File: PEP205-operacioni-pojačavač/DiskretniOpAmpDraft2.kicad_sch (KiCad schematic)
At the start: 40 parts, among them J1 J111, J2 Ulazi, J3 Izlaz, J4 +9V, J5 GND, J6 -9V, J7 KlasaABIzlaz, J8 J111, Q10 NPN, Q11 NPN, Q12 NPN, Q13 NPN, Q14 PNP, Q3 PNP, Q4 PNP, Q5 NPN, Q6 PNP, Q7 PNP, Q8 PNP, Q9 NPN

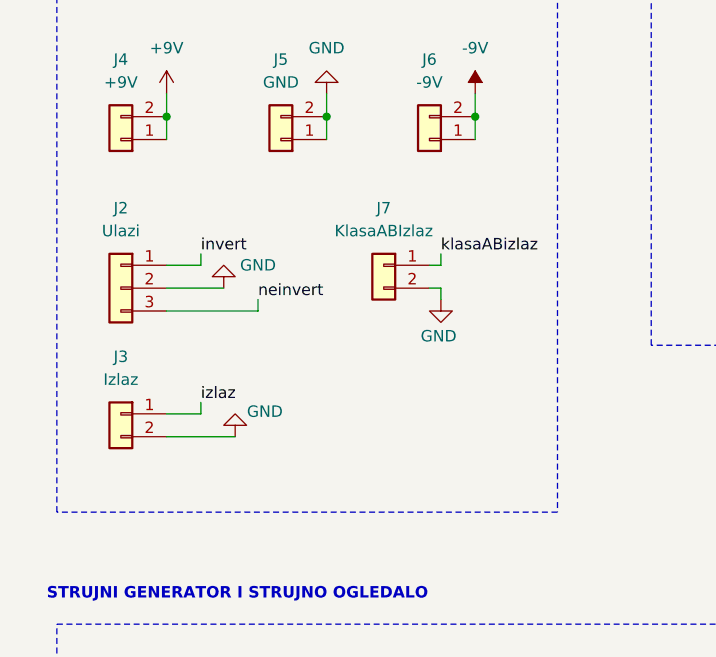
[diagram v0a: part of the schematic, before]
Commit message: zbrzano dodati konektori na drugačiji način
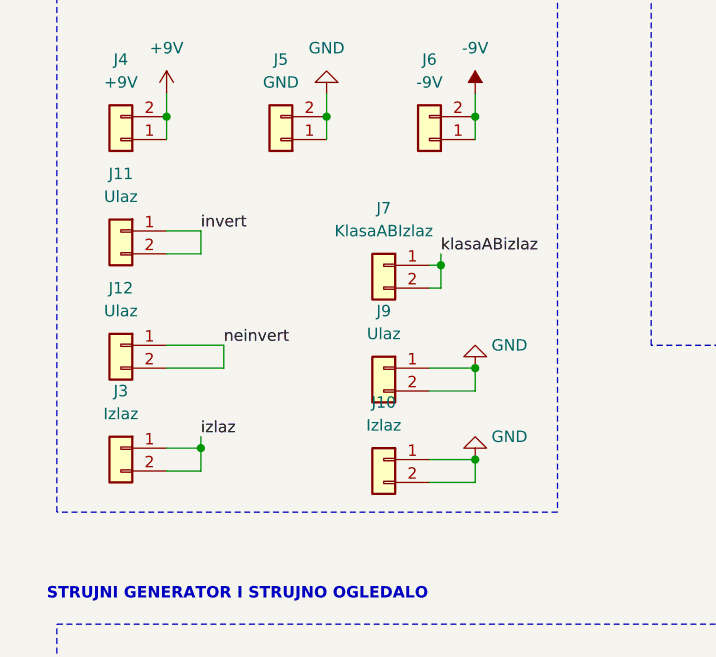
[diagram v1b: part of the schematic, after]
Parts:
- removed J2: Ulazi, Connector_PinSocket_2.54mm:PinSocket_1x03_P2.54mm_Vertical, symbol Connector_Generic:Conn_01x03
- added J10: Izlaz, Connector_PinSocket_2.54mm:PinSocket_1x02_P2.54mm_Vertical, symbol Connector_Generic:Conn_01x02
- added J11, J12, J9: Ulaz, Connector_PinSocket_2.54mm:PinSocket_1x02_P2.54mm_Vertical, symbol Connector_Generic:Conn_01x02
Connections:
- net GND: now also J10.1 (Pin_1), J10.2 (Pin_2), J9.1 (Pin_1), J9.2 (Pin_2); no longer J3.2 (Pin_2), J7.2 (Pin_2)
- net invert: now also J11.1 (Pin_1), J11.2 (Pin_2)
- net izlaz: now also J3.2 (Pin_2)
- net klasaABizlaz: now also J7.2 (Pin_2)
- net neinvert: now also J12.1 (Pin_1), J12.2 (Pin_2)
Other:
- moved on the sheet: J3

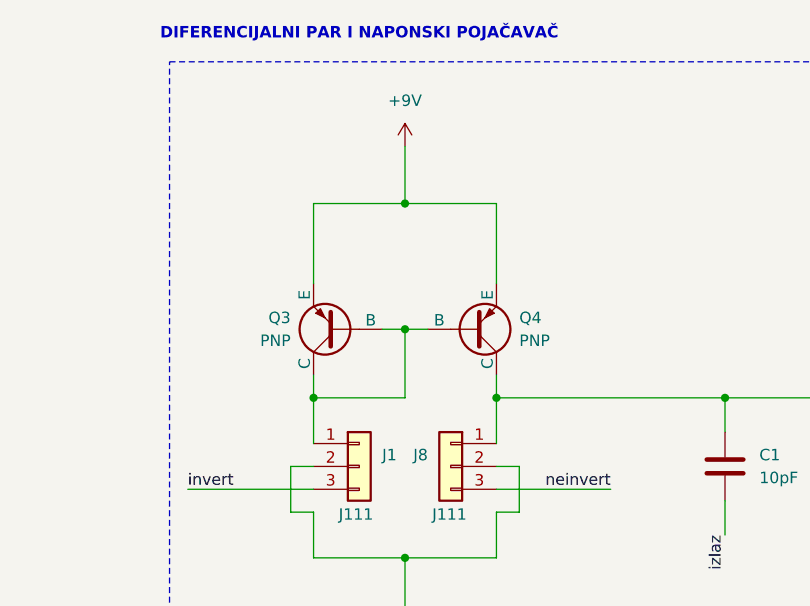
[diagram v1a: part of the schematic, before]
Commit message: Dodat još jedan tranzistor da bi se formiralo Vilsonovo ogledalo sa 3 tranzistora kod diferencijalnog para
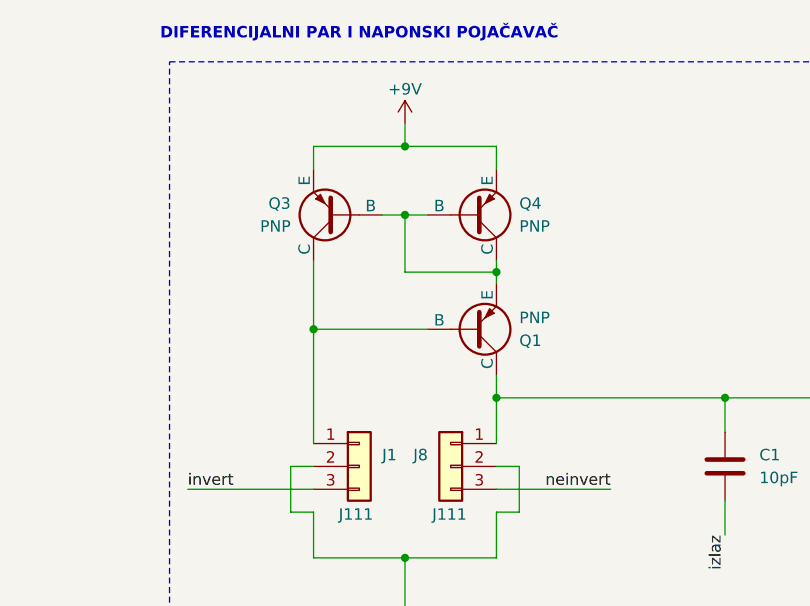
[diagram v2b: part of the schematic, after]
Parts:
- added Q1: PNP, Package_TO_SOT_THT:TO-92, symbol Simulation_SPICE:PNP
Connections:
- net at C1.1, J8.1 (Pin_1), Q5.2 (B): now also Q1.1 (C); no longer Q4.1 (C)
- net at J1.1 (Pin_1), Q3.1 (C): now also Q1.2 (B); no longer Q3.2 (B), Q4.2 (B)
- new net: Q1.3 (E), Q3.2 (B), Q4.1 (C), Q4.2 (B)
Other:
- moved on the sheet: Q3, Q4

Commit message: changed some footprints, some BL traces
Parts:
- Q10, Q3, Q5, Q9: footprint Package_TO_SOT_THT:TO-92 -> Package_TO_SOT_THT:TO-92L_Inline
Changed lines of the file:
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@@
 			)
 		)
-		(property "Footprint" "Package_TO_SOT_THT:TO-92"
+		(property "Footprint" "Package_TO_SOT_THT:TO-92L_Inline"
 			(at 289.56 62.23 0)
 			(hide yes)
@@
 			)
 		)
-		(property "Footprint" "Package_TO_SOT_THT:TO-92"
+		(property "Footprint" "Package_TO_SOT_THT:TO-92L_Inline"
 			(at 13.97 152.4 0)
 			(hide yes)
@@
 			)
 		)
-		(property "Footprint" "Package_TO_SOT_THT:TO-92"
+		(property "Footprint" "Package_TO_SOT_THT:TO-92L_Inline"
 			(at 130.81 41.91 0)
 			(hide yes)
@@
 			)
 		)
-		(property "Footprint" "Package_TO_SOT_THT:TO-92"
+		(property "Footprint" "Package_TO_SOT_THT:TO-92L_Inline"
 			(at 158.75 152.4 0)
 			(hide yes)
